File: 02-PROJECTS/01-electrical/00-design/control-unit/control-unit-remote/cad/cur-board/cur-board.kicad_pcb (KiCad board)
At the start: 2 copper layers, 118 x 56 mm, 31 parts, among them J1 plate cable header 2x6 shroud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, J2 wink lead header 1x5 (L3-S1 9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, J4 screen knob lead header (STEM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, SW1 key - hatch, SW2 key - fuel door, SW3 wink - left (P204), SW4 wink - right (P204), SW5 hazard - latching (P226), U1 IS31FL3218-QFLS2-TR

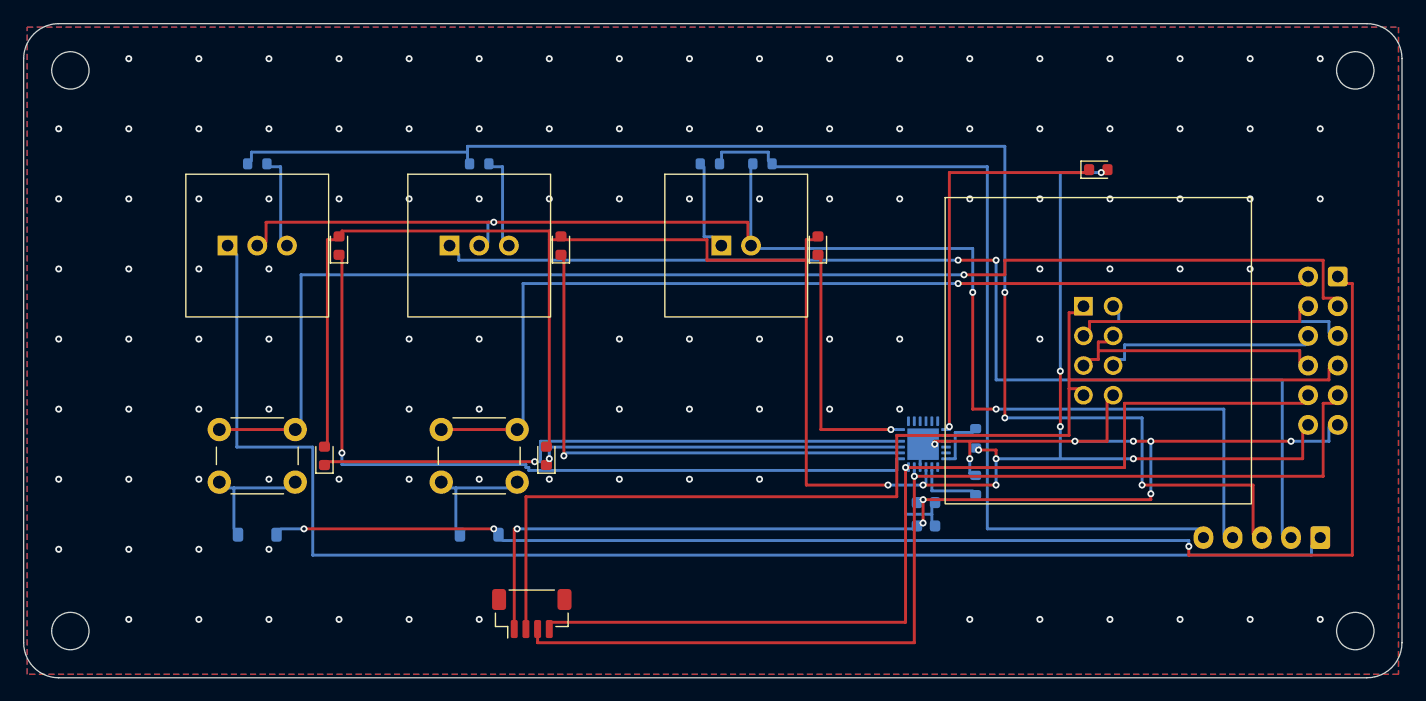
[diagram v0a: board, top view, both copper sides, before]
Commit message: 00-design: the CUR's CAD - board rev 1.00, the box mock-up, every CUR drawing current (D-615)
cur-board rev 1.00: 38.11 x 27.0, four layers, ERC 0, DRC 0 / 0 unconnected /
0 parity, check.py 26 checks 0 mismatches; fab package (16 files), assembly
drawings, BOM, schematic SVG. cur-assembly: shell 41.91 x 30.8 x 19.6, fit check
clear, self-test 13 of 13, four views. READMEs rewritten; plan sheets redrawn.

Co-Authored-By: Claude Opus 5.5 <noreply@anthropic.com>
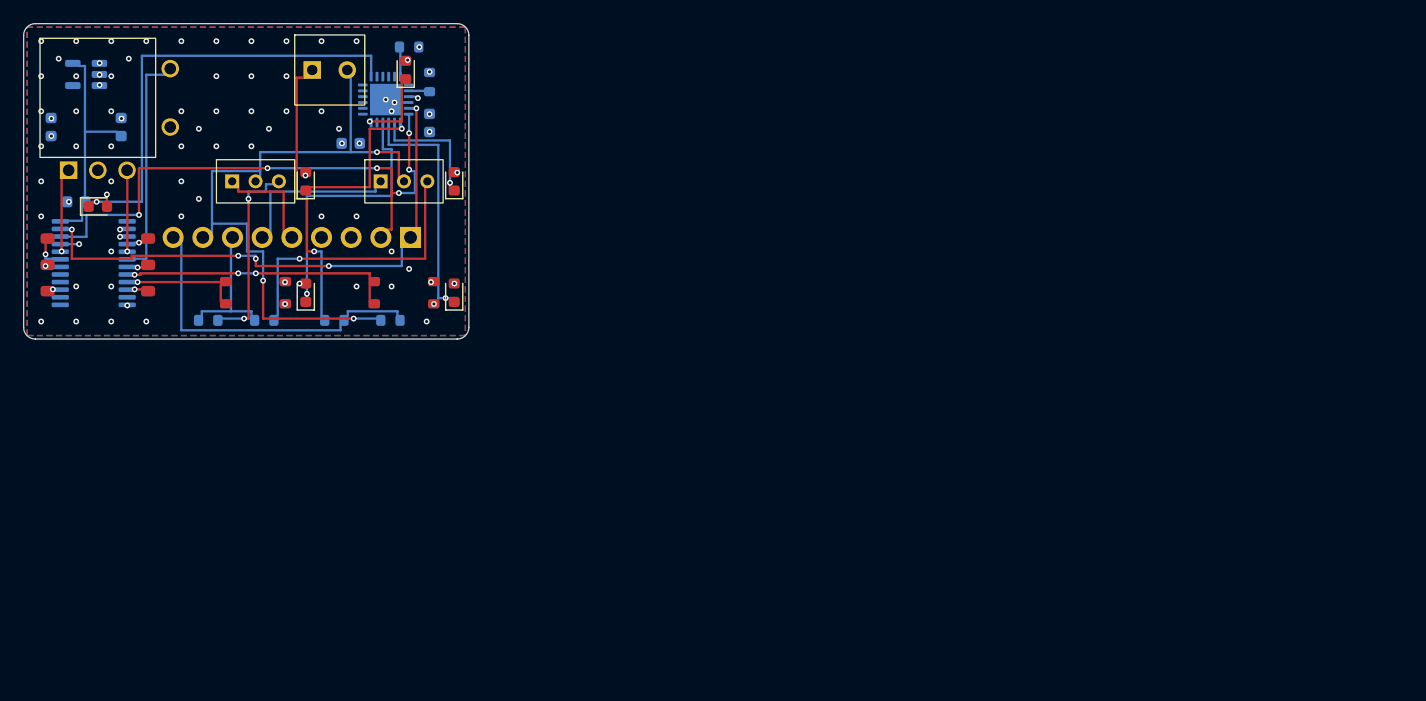
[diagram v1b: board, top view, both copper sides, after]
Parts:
- removed D1, D2: 1N4148W, Diode_SMD:D_SOD-123
- removed H1, H2, H3, H4: M3, MountingHole:MountingHole_3.2mm_M3
- removed J2: wink lead header 1x5 (L3-S1 9 / 10 / 11, commons, L3-S1 6), Connector_JST:JST_XH_B5B-XH-A_1x05_P2.50mm_Vertical
- removed J4: screen knob lead header (STEMMA QT, P219), Connector_JST:JST_SH_BM04B-SRSS-TB_1x04-1MP_P1.00mm_Vertical
- removed JS1: mirror stick (P156) - placeholder, cur-board:Thumbstick_P156_Placeholder_2x04_P2.54mm
- removed KN1: screen knob board (P219), cur-board:ScreenKnob_P219_Board_Placeholder
- added C3: 100nF, Capacitor_SMD:C_0603_1608Metric, B.Cu at (4.50, 15.2)
- added C4: 1uF, Capacitor_SMD:C_0603_1608Metric, B.Cu at (2.35, 8.85)
- added C5: 1uF, Capacitor_SMD:C_0603_1608Metric, B.Cu at (8.35, 8.85)
- added ENC1: screen knob - 9 mm encoder with push (P219), cur-board:ScreenKnob_Encoder9mm_Placeholder, F.Cu at (6.35, 6.35)
- added SW6: mirror control - 4 way + push (P156), cur-board:Thumbstick_SKRH_4Way_Push_Placeholder, F.Cu at (6.35, 20.6)
- added U2: PCA9555PW, Package_SO:TSSOP-24_4.4x7.8mm_P0.65mm, B.Cu at (6.00, 20.5)
- added U3: AP2112K-3.3TRG1, Package_TO_SOT_SMD:SOT-23-5, B.Cu at (5.35, 4.35)
- J1: value plate cable header 2x6 shrouded (DP-DCU-E 1-12, P200) -> pigtail solder pads 1x9 (DP-CUR 1-9); footprint Connector_IDC:IDC-Header_2x06_P2.54mm_Vertical -> cur-board:Pigtail_SolderPads_1x09_P2.54mm
- LED5: value LED 0603 - mirror stick symbol (OUT13) -> LED 0603 - mirror symbol, in the control's well (OUT13)
- SW1, SW2: footprint Button_Switch_THT:SW_PUSH_6mm -> cur-board:SW_PUSH_TL3342_Placeholder
- moved LED5 85.7 mm to (6.35, 15.6)
- moved J1 79.5 mm to (33.1, 18.3)
- moved C1 59.1 mm to (28.0, 10.2)
- moved R2 58.9 mm to (33.0, 2.00), turned to 180 degrees
- moved R1 58.1 mm to (34.8, 5.00)
- moved U1 54.6 mm to (31.0, 6.50), turned to 180 degrees
- moved C2 53.5 mm to (34.8, 8.50), turned to 90 degrees
- moved LED6 38.4 mm to (32.7, 3.97)
- moved SW5 37.9 mm to (26.2, 3.97)
- moved R5 34.8 mm to (26.6, 25.4)
- moved R6 34.6 mm to (31.4, 25.4)
- moved R4 22.8 mm to (20.6, 25.4)
- moved LED3 16.0 mm to (36.9, 23.0)
- moved LED4 14.1 mm to (24.2, 23.0)
- moved R3 14.0 mm to (15.8, 25.4)
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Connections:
- J1 pad 1: /ROW1 -> /PNL_SDA
- J1 pad 2: /COL2 -> /PNL_SCL
- J1 pad 3: /COL3 -> GND
- J1 pad 4: /JOY_X -> /+5V_PNL
- J1 pad 5: /JOY_Y -> /WINK_L_NC
- J1 pad 6: /JOY_PRESS -> /WINK_R_NC
- J1 pad 7: +3V3 -> /WINK_REQ
- J1 pad 8: /AGND -> /WINK_COM
- J1 pad 9: /PNL_SDA -> /HAZ_LADDER
- SW1 pad 1: /COL2 -> /KEY_HATCH
- SW1 pad 2: /KEY_HATCH -> GND
- SW2 pad 1: /COL3 -> /KEY_FUEL
- SW2 pad 2: /KEY_FUEL -> GND
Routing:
- net /+5V_PNL: track 184.8 -> 1.38 mm, vias 9 -> 13
- net /ROW1: track 116.0 -> 0.00 mm, vias 3 -> 0
- net GND: track 114.2 -> 1.88 mm, vias 124 -> 74
- net /WINK_L_NC: track 118.5 -> 7.75 mm
- net /WINK_REQ: track 121.0 -> 10.5 mm, vias 3 -> 0
- net /COL3: track 110.5 -> 0.00 mm, vias 1 -> 0
- net /COL2: track 83.5 -> 0.00 mm, vias 1 -> 0
- net /WINK_R_NC: track 94.5 -> 12.9 mm, vias 2 -> 0
- net +3V3: track 97.5 -> 17.0 mm
- net /WINK_COM: track 116.8 -> 54.5 mm
- net /LED_WINK_L: track 66.8 -> 13.2 mm
- net /HAZ_LADDER: track 73.0 -> 26.6 mm
- net /PNL_SDA: track 89.8 -> 44.5 mm, vias 1 -> 5
- net /LED_WINK_R: track 45.8 -> 10.0 mm
- net /PNL_SCL: track 83.8 -> 48.6 mm, vias 1 -> 6
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- added copper zone on In2.Cu, net /+5V_PNL
- added copper zone on In1.Cu, net GND
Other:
- board size 118 x 56 mm -> 38.1 x 27 mm
- copper layers 2 -> 4
- board text added: "CUR rev 1.00"
- board text added: "DP-CUR 1-9"
- board text removed: "CUR PLATE Y62 rev 0.03"
- board text removed: "D-492 D-499 D-586 D-589 - provisional, confirm"
